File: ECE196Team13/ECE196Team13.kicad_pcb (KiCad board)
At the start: 2 copper layers, 59.6 x 33 mm, 41 parts, among them M1 AO3401A, M2 AO3400A, U1 CN3063-SOIC8, U2 MT3608, U3 SY6280AAC

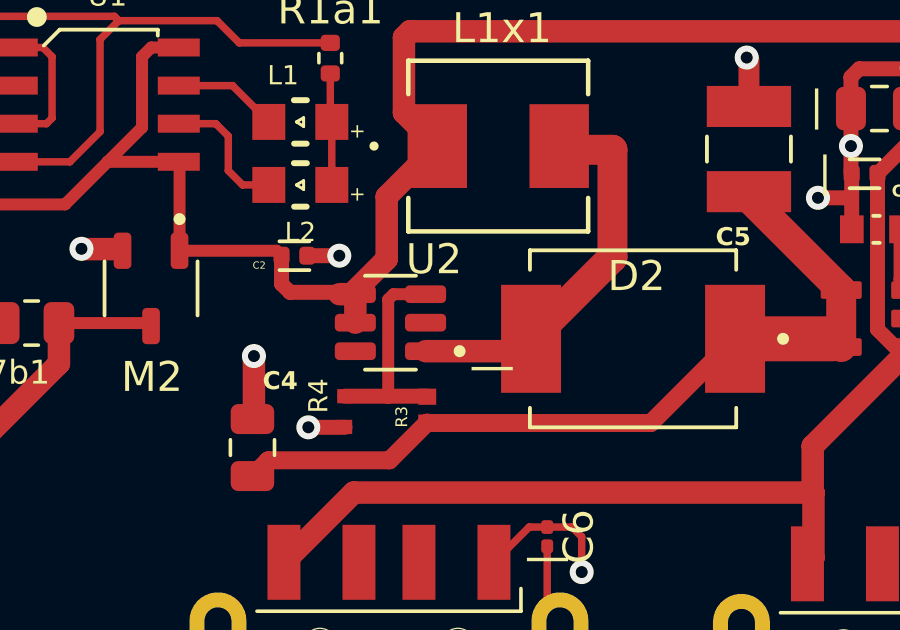
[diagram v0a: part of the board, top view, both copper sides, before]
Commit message: Also fixed. We forgot one connection.
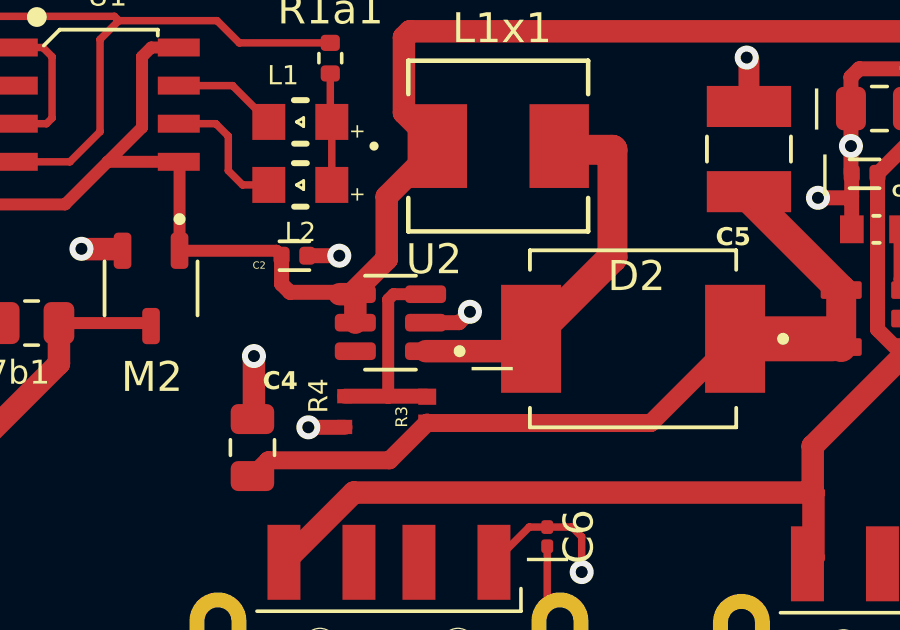
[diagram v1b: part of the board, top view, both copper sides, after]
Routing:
- net GND: track 54.1 -> 55.7 mm, vias 15 -> 16
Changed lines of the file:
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@@
       (drillshape 0)
       (scaleselection 1)
-      (outputdirectory "")
+      (outputdirectory "../../../")
     )
   )
@@
   (segment (start 163.925 53.1) (end 163.925 55.15) (width 0.75) (layer "F.Cu") (net 2))
   (segment (start 151.36 48.045) (end 151.36 46.155) (width 0.25) (layer "F.Cu") (net 2))
+  (segment (start 169.645 51.9875) (end 170.7625 51.9875) (width 0.5) (layer "F.Cu") (net 2))
   (segment (start 159.53 49.575) (end 159.545 49.59) (width 0.25) (layer "F.Cu") (net 2))
   (segment (start 185.85 43.5) (end 185.825 43.525) (width 0.25) (layer "F.Cu") (net 2))
@@
   (segment (start 180.205 45) (end 180.425 44.78) (width 0.25) (layer "F.Cu") (net 2))
   (segment (start 150.925 44.625) (end 150.925 45.5) (width 0.25) (layer "F.Cu") (net 2))
+  (segment (start 170.7625 51.9875) (end 171.125 51.625) (width 0.5) (layer "F.Cu") (net 2))
   (segment (start 138.45 54.35) (end 138.425 54.325) (width 0.25) (layer "F.Cu") (net 2))
   (segment (start 151.415 46.1) (end 151.425 46.1) (width 0.25) (layer "F.Cu") (net 2))
@@
   (via (at 183.825 46.1) (size 0.8) (drill 0.4) (layers "F.Cu" "B.Cu") (net 2))
   (via (at 187.825 50.125) (size 0.8) (drill 0.4) (layers "F.Cu" "B.Cu") (net 2))
+  (via (at 171.125 51.625) (size 0.8) (drill 0.4) (layers "F.Cu" "B.Cu") (free) (net 2))
   (via (at 163.925 53.1) (size 0.8) (drill 0.4) (layers "F.Cu" "B.Cu") (free) (net 2))
   (via (at 165.7375 55.475) (size 0.8) (drill 0.4) (layers "F.Cu" "B.Cu") (free) (net 2))

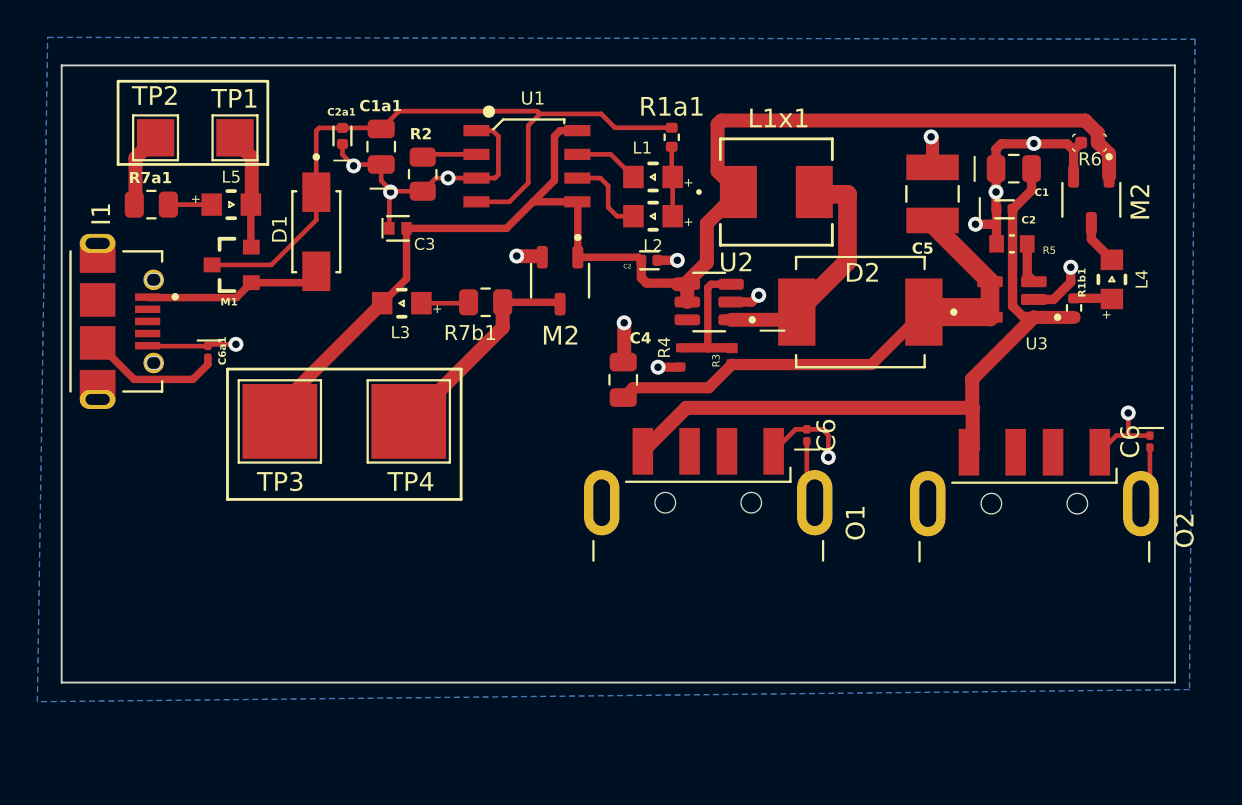
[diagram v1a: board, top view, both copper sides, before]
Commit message: Updates to Solar Battery Stuff
New gerbers, new schematic kind-of (going to make it prettier later), new pcb design. MT3608 and Sy6280AAC layouts should be better.
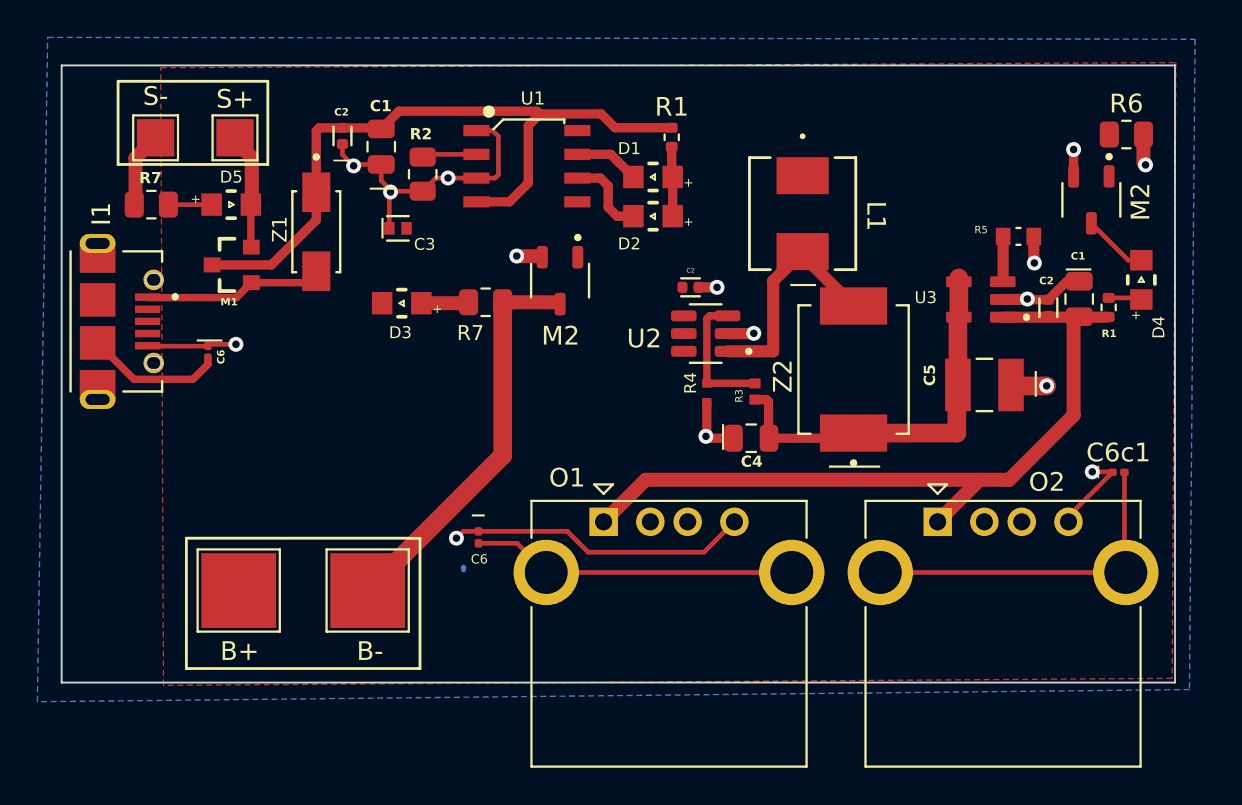
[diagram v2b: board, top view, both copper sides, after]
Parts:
- O1, O2: footprint Connector_USB:USB_A_CNCTech_1001-011-01101_Horizontal -> Connector_USB:USB_A_CONNFLY_DS1095-WNR0
- R6: footprint R6:R0402 -> Resistor_SMD:R_0805_2012Metric
- moved C6 18.4 mm to (156.1, 64.6), turned to 90 degrees
- moved C5 10.6 mm to (183.2, 56.4), turned to 0 degrees
- moved B- 9.31 mm to (150.2, 67.4)
- moved B+ 9.31 mm to (143.3, 67.4)
- moved O1 8.12 mm to (162.8, 63.7), turned to 0 degrees
- moved O2 7.87 mm to (180.7, 63.7), turned to 0 degrees
- moved C1 7.80 mm to (188.3, 51.8), turned to 90 degrees
- moved C4 7.53 mm to (170.7, 59.3), turned to 180 degrees
- moved C2 5.77 mm to (186.6, 52.3), turned to 90 degrees
- moved Z2 3.10 mm to (176.2, 55.6), turned to 90 degrees
- moved C2 2.63 mm to (167.5, 51.2)
- moved R4 2.36 mm to (168.3, 56.9)
- moved C6c1 2.35 mm to (190.4, 61.1), turned to 0 degrees
- moved R3 2.25 mm to (170.9, 56.8)
- moved R6 2.02 mm to (190.8, 43.0), turned to 0 degrees
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- renumbered TP3 to B+, TP4 to B-, C1a1 to C1, C2a1 to C2, C6a1 to C6, C6 to C6c1, L1 to D1, L2 to D2, L3 to D3, L4 to D4, L5 to D5, L1x1 to L1, R1b1 to R1, R1a1 to R1, R7a1 to R7, R7b1 to R7, TP1 to S+, TP2 to S-, D1 to Z1, D2 to Z2
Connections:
- C1 pad 1: Net-(O1-GND) -> Net-(O1-VBUS)
- C2 pad 1: Net-(O1-GND) -> Net-(O1-VBUS)
- C6 pad 1: GND -> Net-(O1-Shield)
- C6 pad 2: Net-(O1-Shield) -> GND
- C6c1 pad 1: Net-(O2-Shield) -> GND
- C6c1 pad 2: GND -> Net-(O2-Shield)
- I1 pad S1: Net-(C6a1-Pad1) -> (no net)
- O1 pad 1: GND -> Net-(O1-VBUS)
- O1 pad 4: Net-(O1-GND) -> GND
- O2 pad 1: GND -> Net-(O1-VBUS)
- O2 pad 4: Net-(O1-GND) -> GND
- R1 pad 1: Net-(O1-GND) -> Net-(O1-VBUS)
- U3 pad 1: Net-(O1-GND) -> Net-(O1-VBUS)
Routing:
- net +BATT: track 73.3 -> 0.96 mm
- net Net-(O1-VBUS): track 0.00 -> 42.3 mm
- net Net-(O1-GND): track 39.0 -> 0.00 mm
- net Net-(O2-Shield): track 3.20 -> 18.5 mm
- net Net-(O1-Shield): track 3.50 -> 17.4 mm
- net -BATT: track 11.6 -> 21.5 mm
- net Net-(U3-EN): track 28.3 -> 21.8 mm
- net GND: track 55.7 -> 60.0 mm, vias 16 -> 15
- net Net-(L4-K): track 2.41 -> 3.49 mm
- net Net-(U2-SW): track 13.5 -> 12.5 mm
- added copper zone on F.Cu, net +BATT
